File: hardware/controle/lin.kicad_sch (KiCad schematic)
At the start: 8 parts, among them J2 Serial, U1 MCP2003B

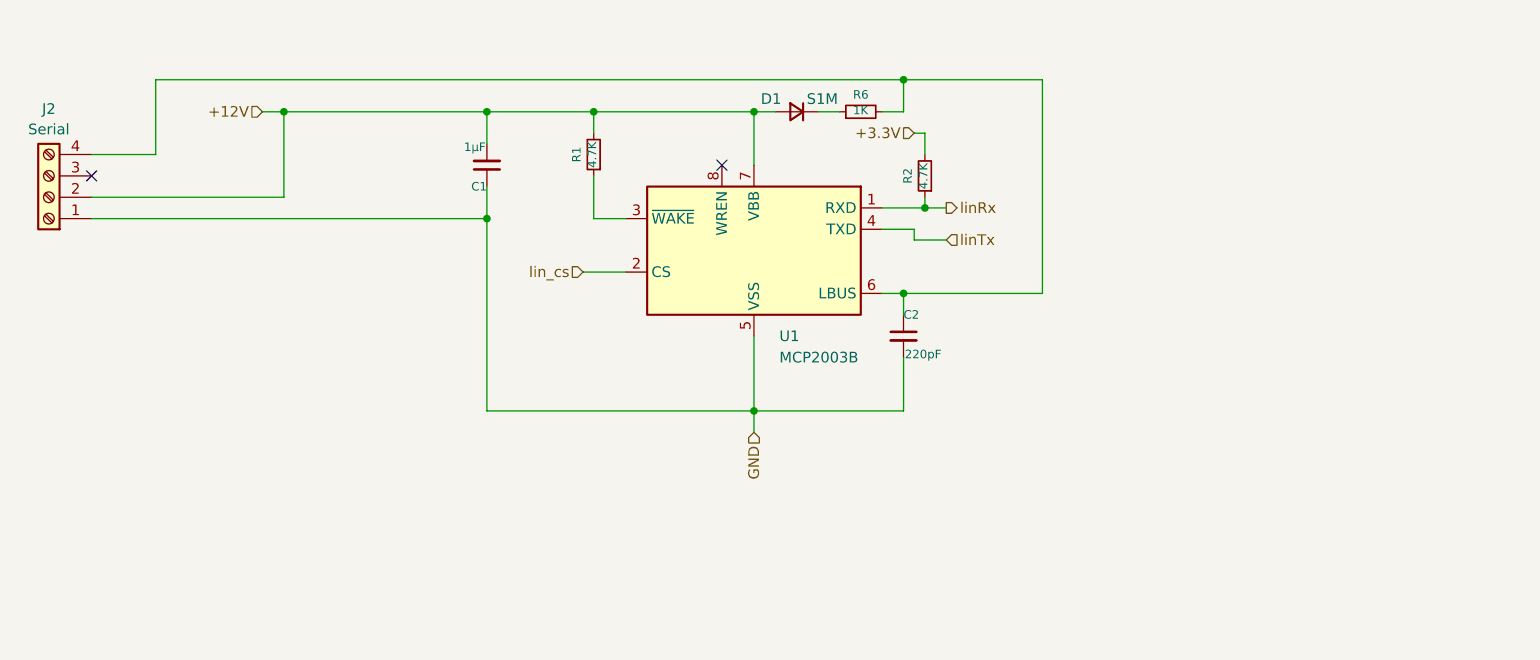
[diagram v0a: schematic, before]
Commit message: controle: add P-MOS transistors to control power to the LIN devices
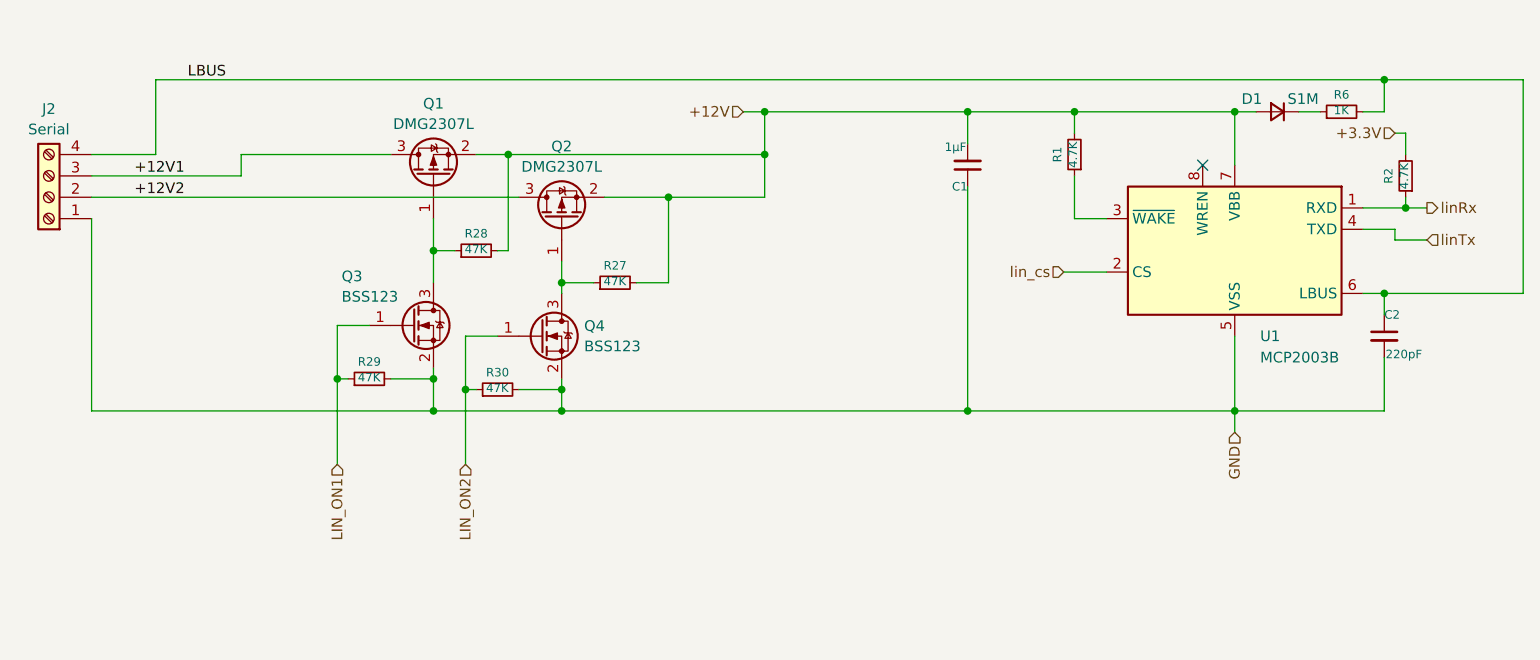
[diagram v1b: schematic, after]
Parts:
- added Q1, Q2: DMG2307L, Package_TO_SOT_SMD:SOT-23, symbol Device:Q_PMOS_GSD
- added Q3, Q4: BSS123, Package_TO_SOT_SMD:SOT-23, symbol Device:Q_NMOS_GSD
- added R27, R28, R29, R30: 47K, Resistor_SMD:R_0805_2012Metric_Pad1.20x1.40mm_HandSolder, symbol Device:R_Small
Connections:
- net +12V: now also Q1.2 (S), Q2.2 (S), R27.2, R28.2; no longer J2.2 (Pin_2)
- net GND: now also Q3.2 (S), Q4.2 (S), R29.2, R30.2
- net LBUS: now reaches C2.1, J2.4 (Pin_4), R6.2, U1.6 (LBUS)
- net +12V1: now reaches J2.3 (Pin_3)
- net +12V1: now also Q1.3 (D)
- new net: Q1.1 (G), Q3.3 (D), R28.1
- new net: Q2.1 (G), Q4.3 (D), R27.1
- new net +12V2: J2.2 (Pin_2), Q2.3 (D)
- new net LIN_ON1: Q3.1 (G), R29.1
- new net LIN_ON2: Q4.1 (G), R30.1
- no-connect marks 2 -> 1
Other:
- moved on the sheet: C1, C2, D1, R1, R2, R6, U1

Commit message: controle: - add leds for LIN power - add optional led for LIN activity - fix lime2 mounting holes - other misc cleanups
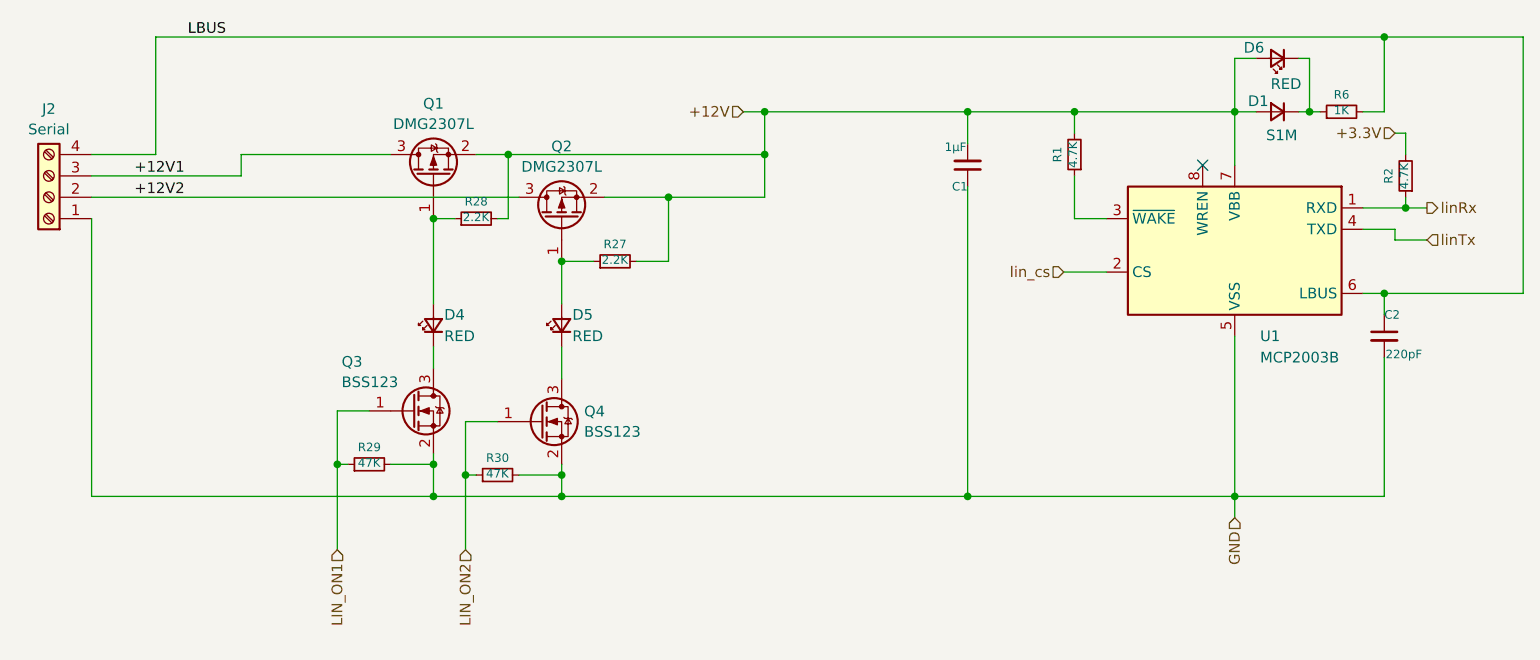
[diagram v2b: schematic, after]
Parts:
- added D4, D5, D6: RED, LED_SMD:LED_0603_1608Metric_Pad1.05x0.95mm_HandSolder, symbol Device:LED_Small
- R27, R28: value 47K -> 2.2K
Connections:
- net +12V: now also D6.2 (A)
- net at Q1.1 (G), R28.1: now also D4.2 (A); no longer Q3.3 (D)
- net at Q2.1 (G), R27.1: now also D5.2 (A); no longer Q4.3 (D)
- net at D1.1 (K), R6.1: now also D6.1 (K)
- new net: D4.1 (K), Q3.3 (D)
- new net: D5.1 (K), Q4.3 (D)
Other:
- moved on the sheet: Q3, Q4, R27, R28, R29, R30

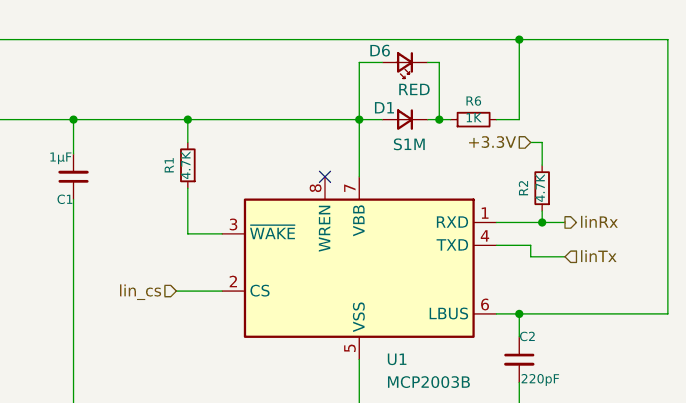
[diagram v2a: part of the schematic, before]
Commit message: controle: fix orioentation of rs232 module connector
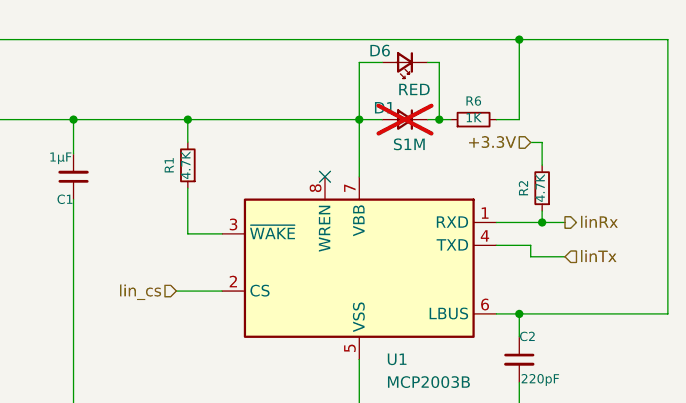
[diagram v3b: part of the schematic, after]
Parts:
- D1: now not fitted
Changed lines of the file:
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@@
 		(in_bom yes)
 		(on_board yes)
-		(dnp no)
+		(dnp yes)
 		(property "Reference" "D1"
 			(at 189.484 50.8 0)

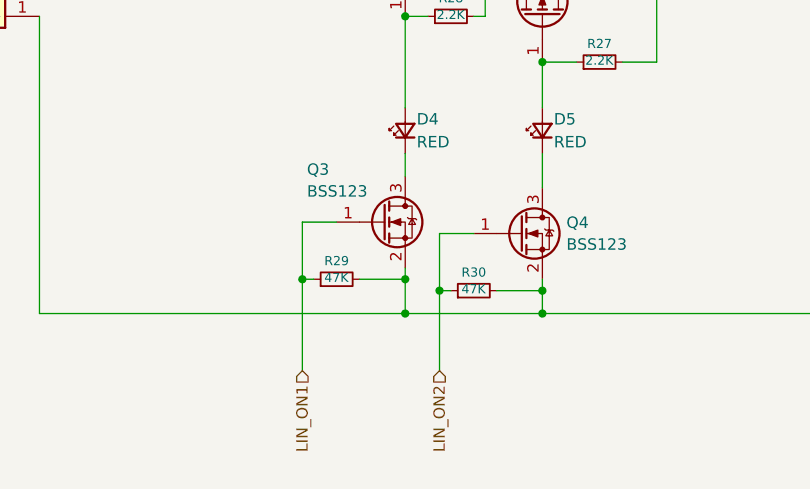
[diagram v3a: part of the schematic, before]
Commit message: hardware/controle: control CPU power from pic18: - add a separate 3.3V power for pic18 - use the pic18 to start the tps54228
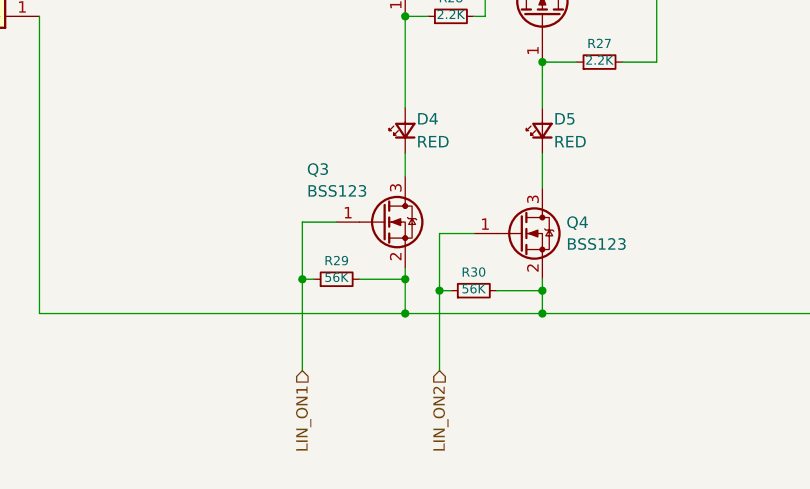
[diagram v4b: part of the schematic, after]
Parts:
- R29, R30: value 47K -> 56K
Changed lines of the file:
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@@
 			)
 		)
-		(property "Value" "47K"
+		(property "Value" "56K"
 			(at 83.7946 93.8022 90)
 			(effects
@@
 			)
 		)
-		(property "Value" "47K"
+		(property "Value" "56K"
 			(at 99.0346 95.0722 90)
 			(effects

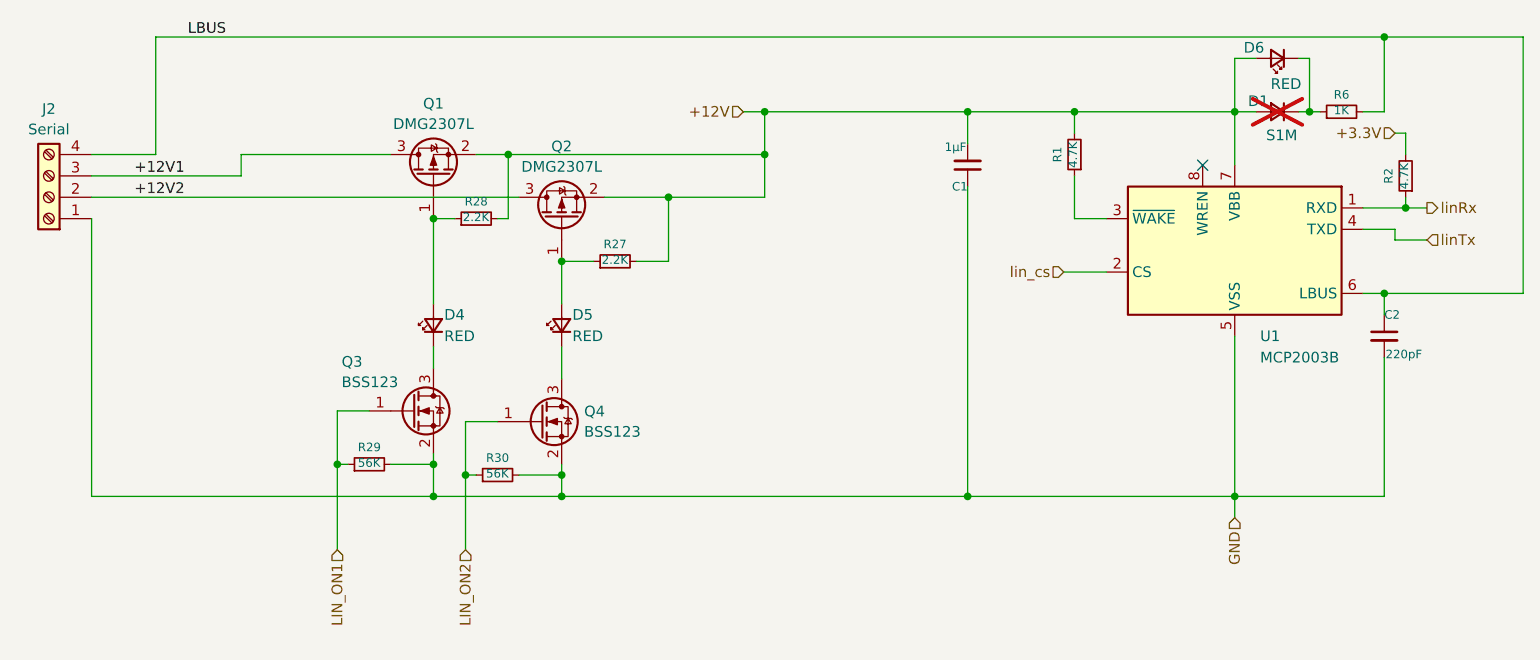
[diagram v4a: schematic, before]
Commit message: hardware/controle: route control CPU power from pic18
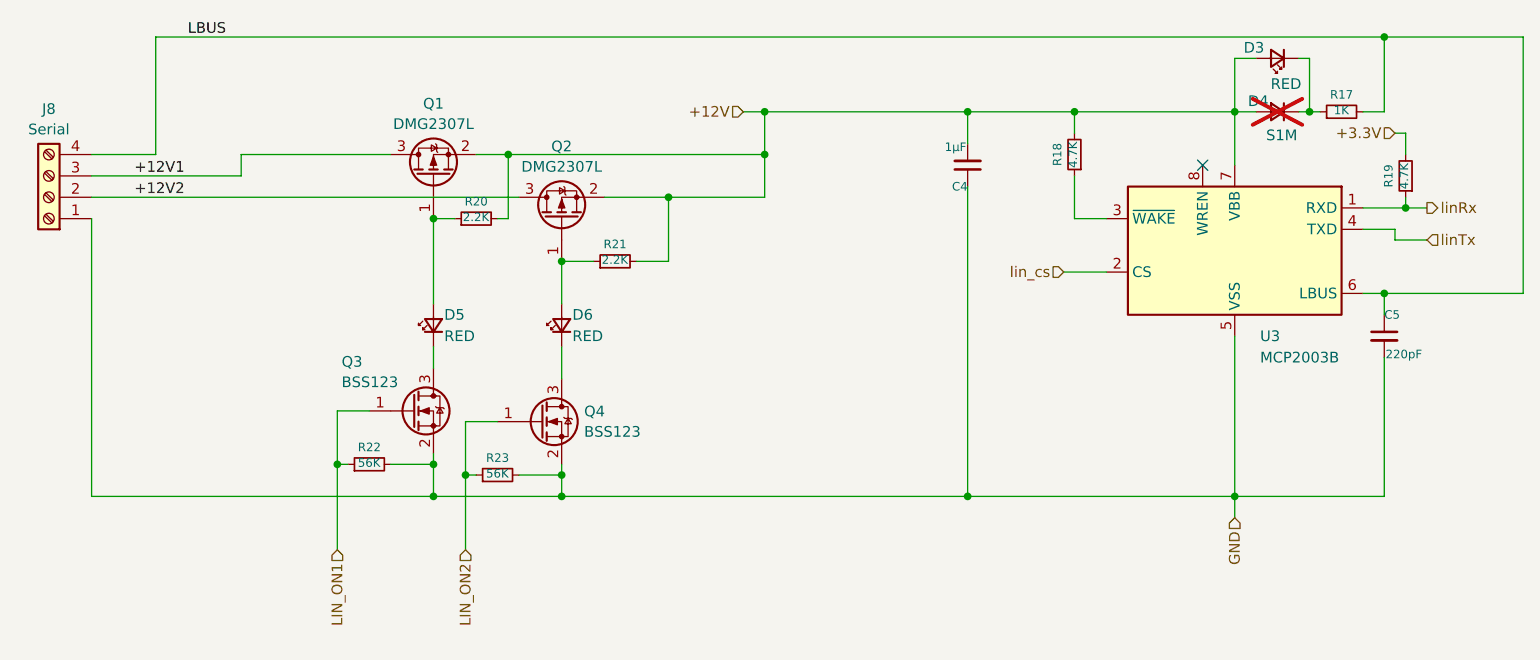
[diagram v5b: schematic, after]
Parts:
- renumbered C1 to C4, C2 to C5, D6 to D3, D1 to D4, D4 to D5, D5 to D6, J2 to J8, R6 to R17, R1 to R18, R2 to R19, R28 to R20, R27 to R21, R29 to R22, R30 to R23, U1 to U3
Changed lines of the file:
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@@
 		(on_board yes)
 		(dnp no)
-		(property "Reference" "C2"
+		(property "Reference" "C5"
 			(at 204.47 76.2 0)
 			(effects
@@
 			(project "controle"
 				(path "/41099c3f-2f7d-470d-b75f-9309d43eb2d2/84cd3668-0fe7-4e30-b793-dfb1a48fec40"
-					(reference "C2")
+					(reference "C5")
 					(unit 1)
 				)
@@
 		(on_board yes)
 		(dnp no)
-		(property "Reference" "R29"
+		(property "Reference" "R22"
 			(at 83.82 91.948 90)
 			(effects
@@
 			(project "controle"
 				(path "/41099c3f-2f7d-470d-b75f-9309d43eb2d2/84cd3668-0fe7-4e30-b793-dfb1a48fec40"
-					(reference "R29")
+					(reference "R22")
 					(unit 1)
 				)
@@
 		(on_board yes)
 		(dnp no)
-		(property "Reference" "R6"
+		(property "Reference" "R17"
 			(at 199.39 50.038 90)
 			(effects
@@
 			(project "controle"
 				(path "/41099c3f-2f7d-470d-b75f-9309d43eb2d2/84cd3668-0fe7-4e30-b793-dfb1a48fec40"
-					(reference "R6")
+					(reference "R17")
 					(unit 1)
 				)
@@
 		(on_board yes)
 		(dnp no)
-		(property "Reference" "D4"
+		(property "Reference" "D5"
 			(at 92.71 76.2 90)
 			(effects
@@
 			(project ""
 				(path "/41099c3f-2f7d-470d-b75f-9309d43eb2d2/84cd3668-0fe7-4e30-b793-dfb1a48fec40"
-					(reference "D4")
+					(reference "D5")
 					(unit 1)
 				)
@@
 		(dnp no)
 		(fields_autoplaced yes)
-		(property "Reference" "U1"
+		(property "Reference" "U3"
 			(at 189.7065 78.74 0)
 			(effects
@@
 			(project "controle"
 				(path "/41099c3f-2f7d-470d-b75f-9309d43eb2d2/84cd3668-0fe7-4e30-b793-dfb1a48fec40"
-					(reference "U1")
+					(reference "U3")
 					(unit 1)
 				)
@@
 		(on_board yes)
 		(dnp no)
-		(property "Reference" "R1"
+		(property "Reference" "R18"
 			(at 165.608 57.15 90)
 			(effects
@@
 			(project "controle"
 				(path "/41099c3f-2f7d-470d-b75f-9309d43eb2d2/84cd3668-0fe7-4e30-b793-dfb1a48fec40"
-					(reference "R1")
+					(reference "R18")
 					(unit 1)
 				)
@@
 		(on_board yes)
 		(dnp no)
-		(property "Reference" "C1"
+		(property "Reference" "C4"
 			(at 154.94 60.96 0)
 			(effects
@@
 			(project "controle"
 				(path "/41099c3f-2f7d-470d-b75f-9309d43eb2d2/84cd3668-0fe7-4e30-b793-dfb1a48fec40"
-					(reference "C1")
+					(reference "C4")
 					(unit 1)
 				)
@@
 		(on_board yes)
 		(dnp no)
-		(property "Reference" "R28"
+		(property "Reference" "R20"
 			(at 96.52 62.738 90)
 			(effects
@@
 			(project "controle"
 				(path "/41099c3f-2f7d-470d-b75f-9309d43eb2d2/84cd3668-0fe7-4e30-b793-dfb1a48fec40"
-					(reference "R28")
+					(reference "R20")
 					(unit 1)
 				)
@@
 		(on_board yes)
 		(dnp no)
-		(property "Reference" "R27"
+		(property "Reference" "R21"
 			(at 113.03 67.818 90)
 			(effects
@@
 			(project "controle"
 				(path "/41099c3f-2f7d-470d-b75f-9309d43eb2d2/84cd3668-0fe7-4e30-b793-dfb1a48fec40"
-					(reference "R27")
+					(reference "R21")
 					(unit 1)
 				)
@@
 		(on_board yes)
 		(dnp no)
-		(property "Reference" "D5"
+		(property "Reference" "D6"
 			(at 107.95 76.2 90)
 			(effects
@@
 			(project "controle"
 				(path "/41099c3f-2f7d-470d-b75f-9309d43eb2d2/84cd3668-0fe7-4e30-b793-dfb1a48fec40"
-					(reference "D5")
+					(reference "D6")
 					(unit 1)
 				)
@@
 		(on_board yes)
 		(dnp no)
-		(property "Reference" "D6"
+		(property "Reference" "D3"
 			(at 188.976 44.45 0)
 			(effects
@@
 			(project "controle"
 				(path "/41099c3f-2f7d-470d-b75f-9309d43eb2d2/84cd3668-0fe7-4e30-b793-dfb1a48fec40"
-					(reference "D6")
+					(reference "D3")
 					(unit 1)
 				)
@@
 		(dnp no)
 		(fields_autoplaced yes)
-		(property "Reference" "J2"
+		(property "Reference" "J8"
 			(at 45.72 51.7355 0)
 			(effects
@@
 			(project "controle"
 				(path "/41099c3f-2f7d-470d-b75f-9309d43eb2d2/84cd3668-0fe7-4e30-b793-dfb1a48fec40"
-					(reference "J2")
+					(reference "J8")
 					(unit 1)
 				)
@@
 		(on_board yes)
 		(dnp no)
-		(property "Reference" "R2"
+		(property "Reference" "R19"
 			(at 204.978 59.69 90)
 			(effects
@@
 			(project "controle"
 				(path "/41099c3f-2f7d-470d-b75f-9309d43eb2d2/84cd3668-0fe7-4e30-b793-dfb1a48fec40"
-					(reference "R2")
+					(reference "R19")
 					(unit 1)
 				)
@@
 		(on_board yes)
 		(dnp no)
-		(property "Reference" "R30"
+		(property "Reference" "R23"
 			(at 99.06 93.218 90)
 			(effects
@@
 			(project "controle"
 				(path "/41099c3f-2f7d-470d-b75f-9309d43eb2d2/84cd3668-0fe7-4e30-b793-dfb1a48fec40"
-					(reference "R30")
+					(reference "R23")
 					(unit 1)
 				)
@@
 		(on_board yes)
 		(dnp yes)
-		(property "Reference" "D1"
+		(property "Reference" "D4"
 			(at 189.484 50.8 0)
 			(effects
@@
 			(project "controle"
 				(path "/41099c3f-2f7d-470d-b75f-9309d43eb2d2/84cd3668-0fe7-4e30-b793-dfb1a48fec40"
-					(reference "D1")
-					(unit 1)
-				)
+					(reference "D4")
+					(unit 1)
+				)

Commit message: hardware/controle: update some component values and P/N
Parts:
- D3, D5, D6: P/N (none) -> MP008293
- R17: P/N stock -> MCWR08X1001FTL
- R18, R19: P/N stock -> MCWR08X4701FTL
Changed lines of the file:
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@@
 			)
 		)
-		(property "P/N" "stock"
+		(property "P/N" "MCWR08X1001FTL"
 			(at 199.39 52.07 0)
 			(effects
@@
 		)
 		(property "Description" "Light emitting diode, small symbol"
+			(at 91.44 77.47 0)
+			(effects
+				(font
+					(size 1.27 1.27)
+				)
+				(hide yes)
+			)
+		)
+		(property "P/N" "MP008293"
 			(at 91.44 77.47 0)
 			(effects
@@
 			)
 		)
-		(property "P/N" "stock"
+		(property "P/N" "MCWR08X4701FTL"
 			(at 167.64 57.15 0)
 			(effects
@@
 			)
 		)
+		(property "P/N" "MP008293"
+			(at 106.68 77.47 0)
+			(effects
+				(font
+					(size 1.27 1.27)
+				)
+				(hide yes)
+			)
+		)
 		(pin "2"
 		)
@@
 		)
 		(property "Description" "Light emitting diode, small symbol"
+			(at 191.77 45.72 0)
+			(effects
+				(font
+					(size 1.27 1.27)
+				)
+				(hide yes)
+			)
+		)
+		(property "P/N" "MP008293"
 			(at 191.77 45.72 0)
 			(effects
@@
 			)
 		)
-		(property "P/N" "stock"
+		(property "P/N" "MCWR08X4701FTL"
 			(at 207.01 59.69 0)
 			(effects

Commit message: hardware/controle: update P/N fields
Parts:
- C4: P/N C0805C105K3RACTU ou 08053C105KAT9A (stock) -> C0805C105K3RACTU ou 08053C105KAT9A
- R20, R21: P/N stock -> MCWR08X2201FTL
- R22, R23: P/N stock -> MCWR08X5602FTL
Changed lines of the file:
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@@
 			)
 		)
-		(property "P/N" "stock"
+		(property "P/N" "MCWR08X5602FTL"
 			(at 83.82 93.98 0)
 			(effects
@@
 			)
 		)
-		(property "P/N" "C0805C105K3RACTU ou 08053C105KAT9A (stock)"
+		(property "P/N" "C0805C105K3RACTU ou 08053C105KAT9A"
 			(at 154.94 58.42 0)
 			(effects
@@
 			)
 		)
-		(property "P/N" "stock"
+		(property "P/N" "MCWR08X2201FTL"
 			(at 96.52 64.77 0)
 			(effects
@@
 			)
 		)
-		(property "P/N" "stock"
+		(property "P/N" "MCWR08X2201FTL"
 			(at 113.03 69.85 0)
 			(effects
@@
 			)
 		)
-		(property "P/N" "stock"
+		(property "P/N" "MCWR08X5602FTL"
 			(at 99.06 95.25 0)
 			(effects
